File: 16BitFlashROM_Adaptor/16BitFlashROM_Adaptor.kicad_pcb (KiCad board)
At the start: 2 copper layers, 19.2 x 52.3 mm, 15 parts, among them J2 Right GPIO, J5 Right GPIO, U1 M29F160FT55N3E2

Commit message: - Updated Vic20 Flash Cart files to Ki-CAD 9.x - Cleaned up some component names and generated ibom's
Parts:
- J1: value ~ -> Address
- J2: value Right GPIO -> Right Pins
- J3: value ~ -> Reset
- J5: value Right GPIO -> Left Pins

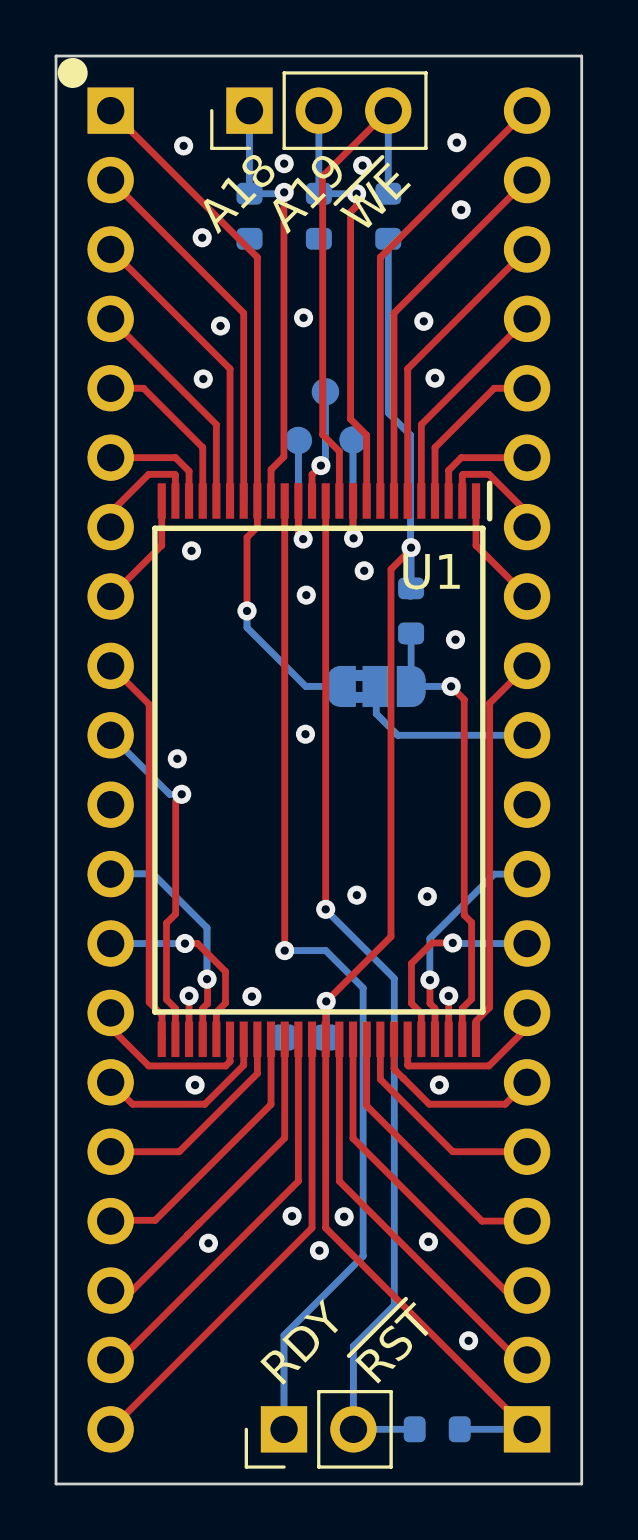
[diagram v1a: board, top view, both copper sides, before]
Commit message: - Added A Couple Of 5v Pins To Easily Jumper The Additional ROM Banks.
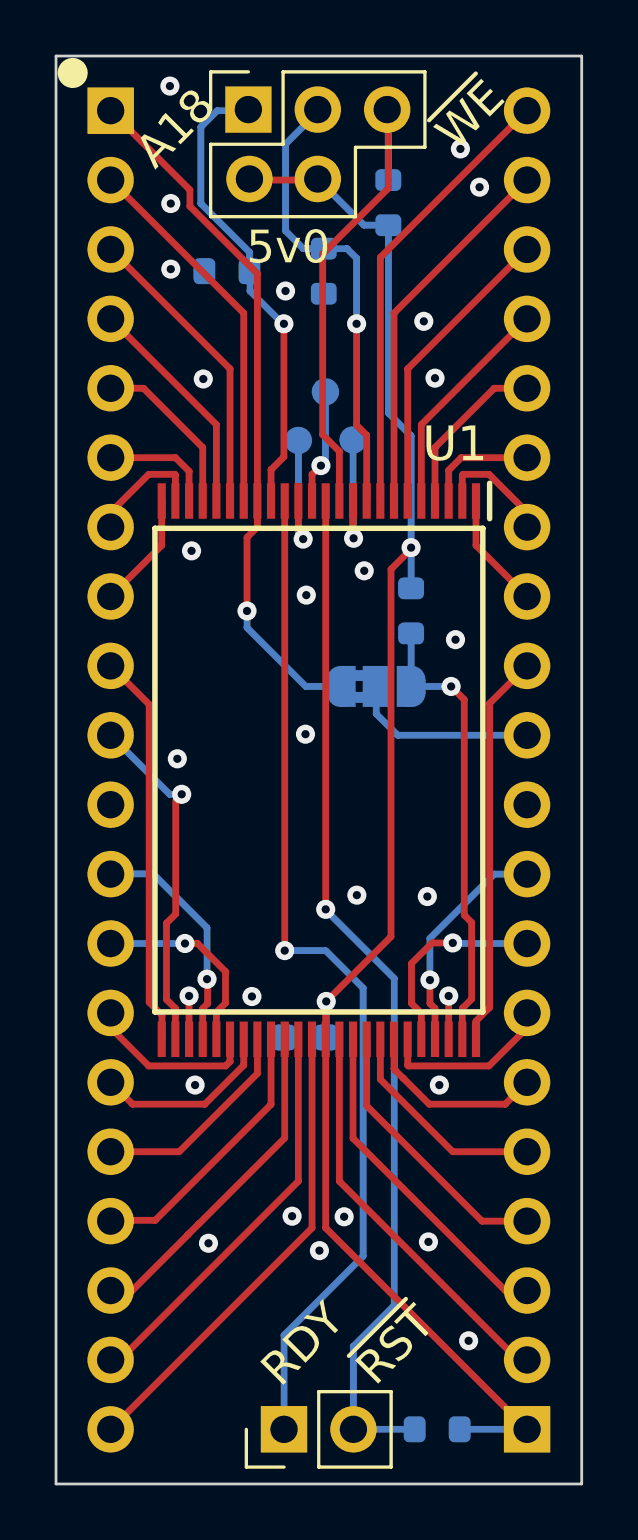
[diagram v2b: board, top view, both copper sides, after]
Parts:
- J1: footprint Connector_PinHeader_2.54mm:PinHeader_1x03_P2.54mm_Vertical -> Dave Footprints:PinHeader_Amiga_ROM
- moved R2 2.17 mm to (144.0, 94.8), turned to 0 degrees
- moved R1 2.02 mm to (147.5, 94.8)
- moved R4 0.50 mm to (149.9, 92.3)
- turned J1 to 0 degrees
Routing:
- net VCC: track 55.3 -> 59.8 mm
- net /A18: track 15.8 -> 17.2 mm
- net /A19: track 15.9 -> 17.2 mm
- net /~{WE}: track 18.6 -> 18.1 mm
- net GND: vias 30 -> 28
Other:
- board text added: "5v0"
- board text removed: "A19"
